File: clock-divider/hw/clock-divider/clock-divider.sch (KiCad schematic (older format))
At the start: 47 parts

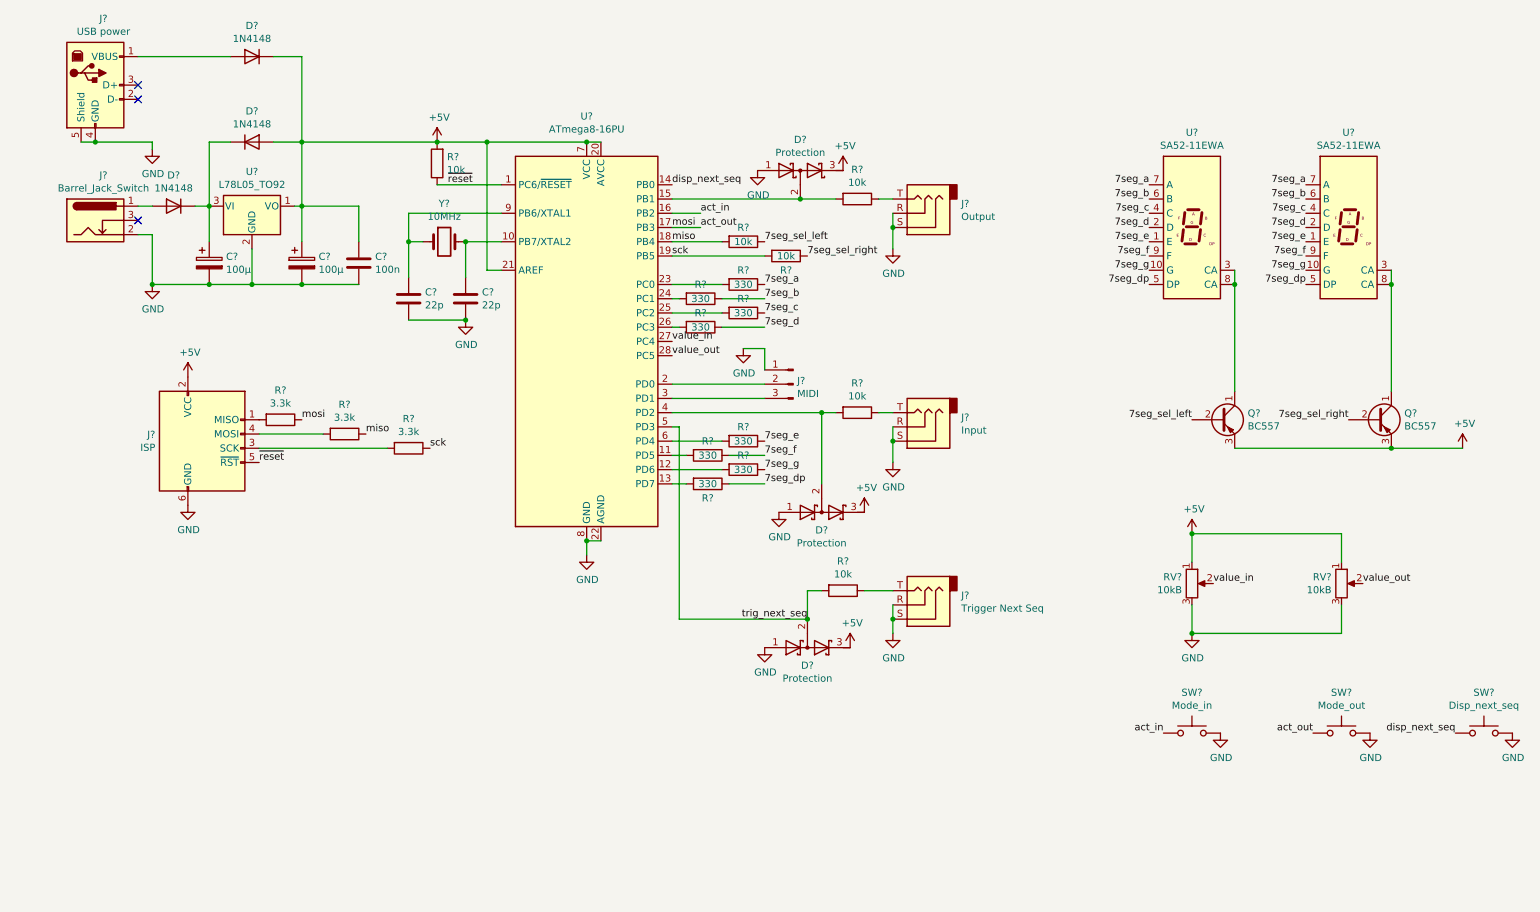
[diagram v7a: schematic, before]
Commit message: clock-divider: hw: cosmetic cleanup
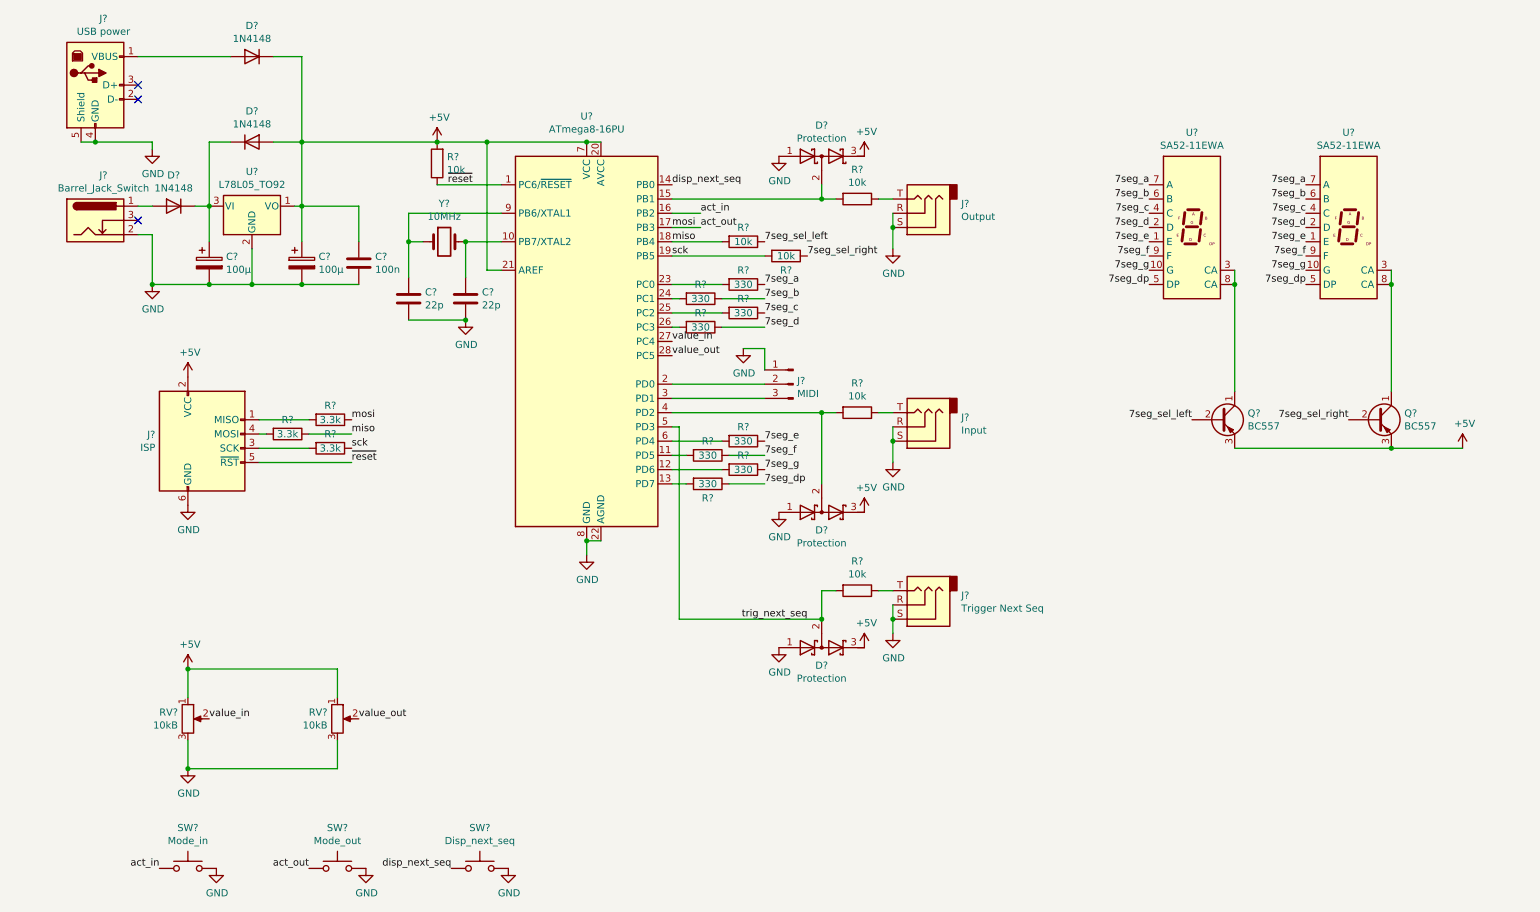
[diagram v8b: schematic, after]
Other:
- moved on the sheet: D?, R?, RV?, SW?
